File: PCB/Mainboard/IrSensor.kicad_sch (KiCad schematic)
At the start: 1 part, among them J3 Conn_01x03_Pin

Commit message: First rev is done
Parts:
- J3: value Conn_01x03_Pin -> UV
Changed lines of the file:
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@@
 			)
 		)
-		(property "Value" "Conn_01x03_Pin"
+		(property "Value" "UV"
 			(at 139.7 110.4899 0)
 			(effects

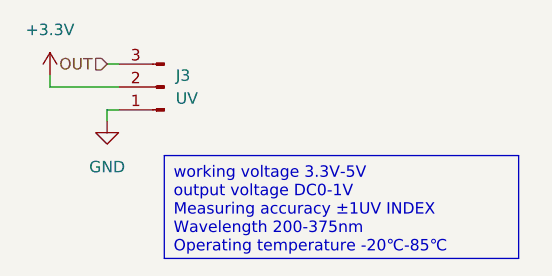
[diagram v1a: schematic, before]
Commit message: updated some resitor values
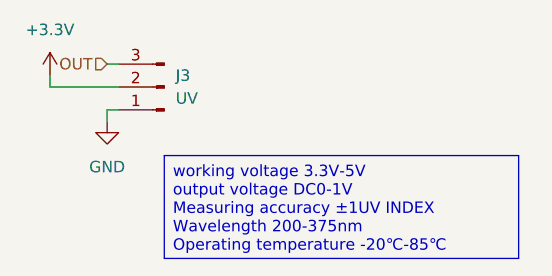
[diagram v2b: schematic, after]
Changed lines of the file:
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@@
 (kicad_sch
-	(version 20231120)
+	(version 20250114)
 	(generator "eeschema")
-	(generator_version "8.0")
+	(generator_version "9.0")
 	(paper "A4")
+	(text_box "working voltage 3.3V-5V\noutput voltage DC0-1V\nMeasuring accuracy ±1UV INDEX\nWavelength 200-375nm\nOperating temperature -20℃-85℃"
+		(exclude_from_sim no)
+		(at 138.43 116.84 0)
+		(size 39.37 11.43)
+		(margins 0.9525 0.9525 0.9525 0.9525)
+		(stroke
+			(width 0)
+			(type default)
+		)
+		(fill
+			(type none)
+		)
+		(effects
+			(font
+				(size 1.27 1.27)
+			)
+			(justify left top)
+		)
+	)
 	(wire
 		(pts
@@
 		)
 	)
-	(text_box "working voltage 3.3V-5V\noutput voltage DC0-1V\nMeasuring accuracy ±1UV INDEX\nWavelength 200-375nm\nOperating temperature -20℃-85℃"
-		(exclude_from_sim no)
-		(at 138.43 116.84 0)
-		(size 39.37 11.43)
-		(stroke
-			(width 0)
-			(type default)
-		)
-		(fill
-			(type none)
-		)
-		(effects
-			(font
-				(size 1.27 1.27)
-			)
-			(justify left top)
-		)
-	)
 	(hierarchical_label "OUT"
 		(shape input)
 		(at 132.08 106.68 180)
-		(fields_autoplaced yes)
 		(effects
 			(font
